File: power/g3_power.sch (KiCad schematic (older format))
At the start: 40 parts, among them J101 533980271_Molex, J102 533980271_Molex, J103 53398-0871, SW1 SW_Push, U101 RT9471GQW, U102 TPS61202DRC, U103 LM358, U104 MCP3422

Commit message: fixes to schematic and layout
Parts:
- added TP101, TP102, TP103, TP104, TP105, TP106, TP107, TP108, TP109, TP110, TP111, TP112, TP113, TP114, TP115: TestPoint, Perch:HARWIN_S2751-46R, symbol Connector:TestPoint
- SW1: symbol Switch:SW_Push -> Switch:SW_DIP_x02
- renumbered R109 to R107, R110 to R108, R111 to R109, R112 to R110
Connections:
- net +5V: now also TP106.1
- net BOOST_PS: now also TP110.1
- net BOOST_VAUX: now also TP101.1
- net CC_PIMD: now also TP104.1
- net CC_PWR_OUT: now also TP102.1
- net CC_SCL: now also TP108.1
- net CC_SDA: now also TP109.1
- net GND: now also SW1.4, TP113.1, TP114.1, TP115.1; no longer H101.1, H102.1, H103.1, H104.1, SW1.2
- net V_BATT: now also TP107.1
- net V_REGN: now also TP105.1
- net V_SOL: now also TP103.1
- net ~CC_CE: now also TP112.1
- net ~CC_INT: now also TP111.1
- no-connect marks 2 -> 8
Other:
- note added: "Test Points"

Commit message: Rerouting power PCB
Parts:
- U102: footprint Package_SON:Texas_S-PVSON-N10_ThermalVias -> digikey-footprints:VSON-10-1EP_3x3mm
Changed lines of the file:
@@
 F 0 "U102" H 9275 3842 50  0000 C CNN
 F 1 "TPS61202DRC" H 9275 3751 50  0000 C CNN
-F 2 "Package_SON:Texas_S-PVSON-N10_ThermalVias" H 9275 2925 50  0001 C CNN
+F 2 "digikey-footprints:VSON-10-1EP_3x3mm" H 9275 2925 50  0001 C CNN
 F 3 "http://www.ti.com/lit/ds/symlink/tps61200.pdf" H 9275 3375 50  0001 C CNN
 	1    9275 3375
@@
 $EndComp
 $Comp
-L custom_power:CC_PWR_OUT #PWR0115
+L g3_power-rescue:CC_PWR_OUT-custom_power #PWR0115
 U 1 1 62098452
 P 1250 6300
@@
 $EndComp
 $Comp
-L custom_power:CC_PWR_OUT #PWR0117
+L g3_power-rescue:CC_PWR_OUT-custom_power #PWR0117
 U 1 1 62098FD7
 P 950 6300
@@
 $EndComp
 $Comp
-L custom_power:CC_PIMD #PWR0121
+L g3_power-rescue:CC_PIMD-custom_power #PWR0121
 U 1 1 620AAC46
 P 2300 6300
@@
 $EndComp
 $Comp
-L custom_power:CC_PWR_OUT #PWR0132
+L g3_power-rescue:CC_PWR_OUT-custom_power #PWR0132
 U 1 1 620C5643
 P 1300 3500
@@
 $EndComp
 $Comp
-L custom_power:CC_PWR_OUT #PWR0133
+L g3_power-rescue:CC_PWR_OUT-custom_power #PWR0133
 U 1 1 620C5BAD
 P 4950 1775
@@
 $EndComp
 $Comp
-L custom_power:BOOST_VAUX #PWR0148
+L g3_power-rescue:BOOST_VAUX-custom_power #PWR0148
 U 1 1 620D33DE
 P 4450 6275
@@
 $EndComp
 $Comp
-L custom_power:BOOST_VAUX #PWR0150
+L g3_power-rescue:BOOST_VAUX-custom_power #PWR0150
 U 1 1 620DC5AE
 P 8000 3425
@@
 $EndComp
 $Comp
-L custom_power:CC_PWR_OUT #PWR0151
+L g3_power-rescue:CC_PWR_OUT-custom_power #PWR0151
 U 1 1 620DD237
 P 8000 3125
@@
 	8000 3475 8875 3475
 $Comp
-L custom_power:BOOST_VAUX #PWR0152
+L g3_power-rescue:BOOST_VAUX-custom_power #PWR0152
 U 1 1 620EE8BF
 P 10100 3225
@@
 	10100 3375 10100 3225
 $Comp
-L custom_power:CC_PWR_OUT #PWR0153
+L g3_power-rescue:CC_PWR_OUT-custom_power #PWR0153
 U 1 1 62018816
 P 1825 3500
@@
 $EndComp
 $Comp
-L custom_power:CC_PIMD #PWR0154
+L g3_power-rescue:CC_PIMD-custom_power #PWR0154
 U 1 1 620415CA
 P 3125 1300
@@
 	5600 6450 5600 6300
 $Comp
-L custom_power:CC_PWR_OUT #PWR0106
+L g3_power-rescue:CC_PWR_OUT-custom_power #PWR0106
 U 1 1 620113D1
 P 5600 6300
@@
 NoConn ~ 5225 5575
 $Comp
-L custom_power:BOOST_VAUX #PWR0155
+L g3_power-rescue:BOOST_VAUX-custom_power #PWR0155
 U 1 1 62184ADE
 P 6200 825
@@
 $EndComp
 $Comp
-L custom_power:CC_PWR_OUT #PWR0156
+L g3_power-rescue:CC_PWR_OUT-custom_power #PWR0156
 U 1 1 621D276E
 P 6200 1100
@@
 $EndComp
 $Comp
-L custom_power:CC_PIMD #PWR0158
+L g3_power-rescue:CC_PIMD-custom_power #PWR0158
 U 1 1 62224531
 P 6200 1700

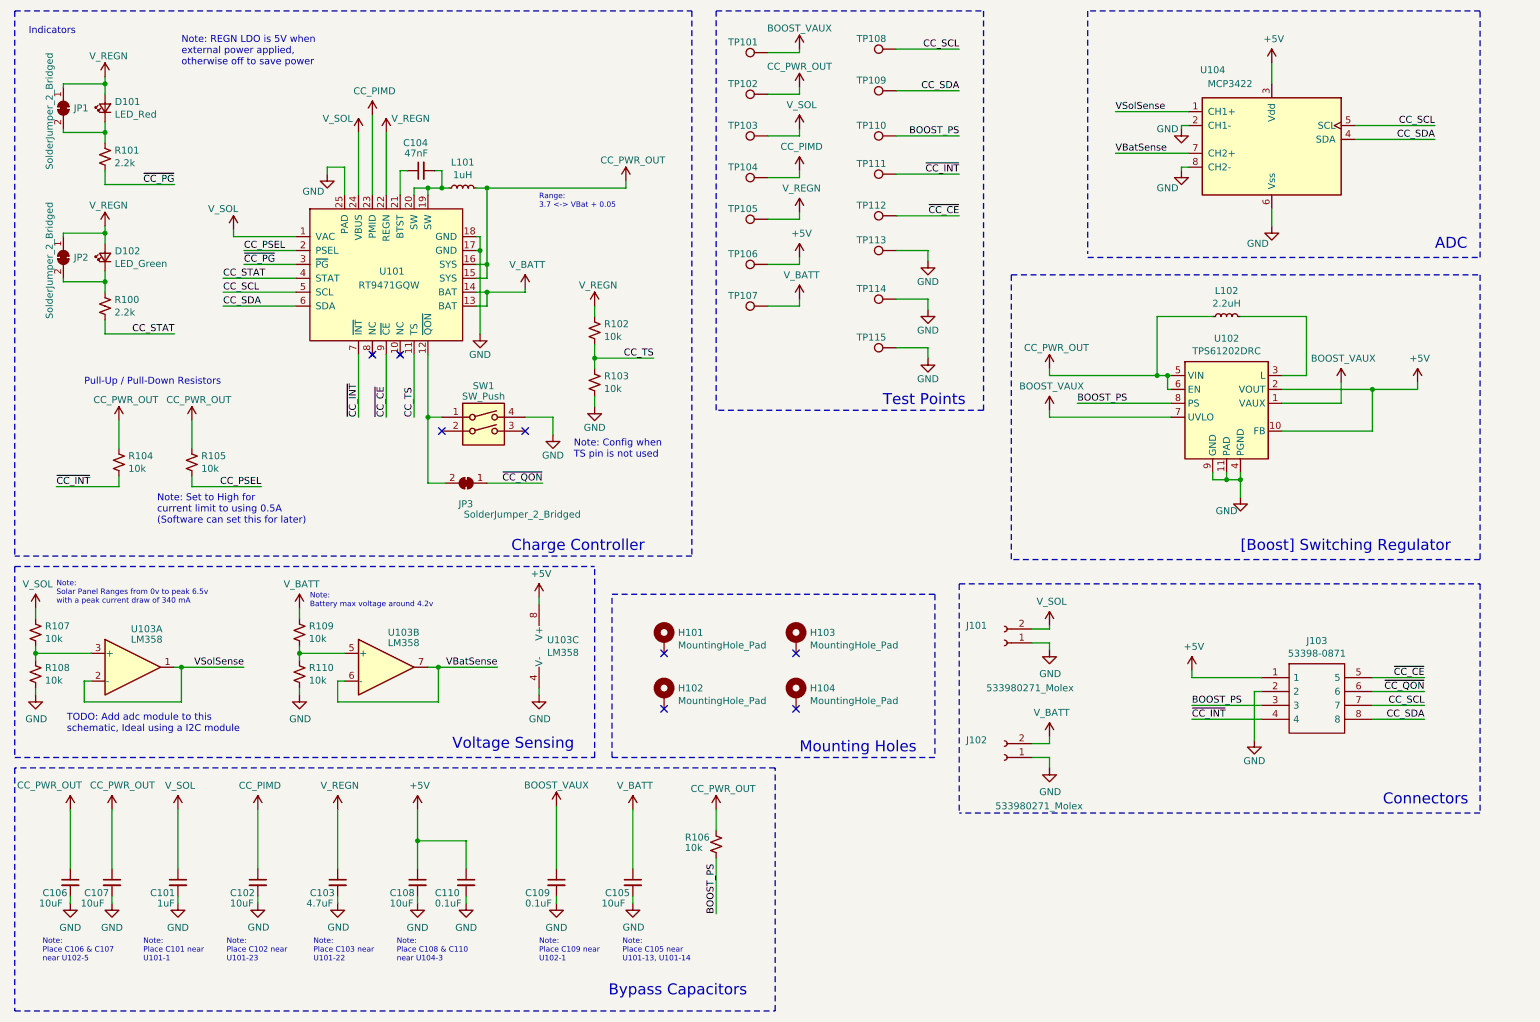
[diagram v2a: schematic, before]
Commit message: Labeling testpoints
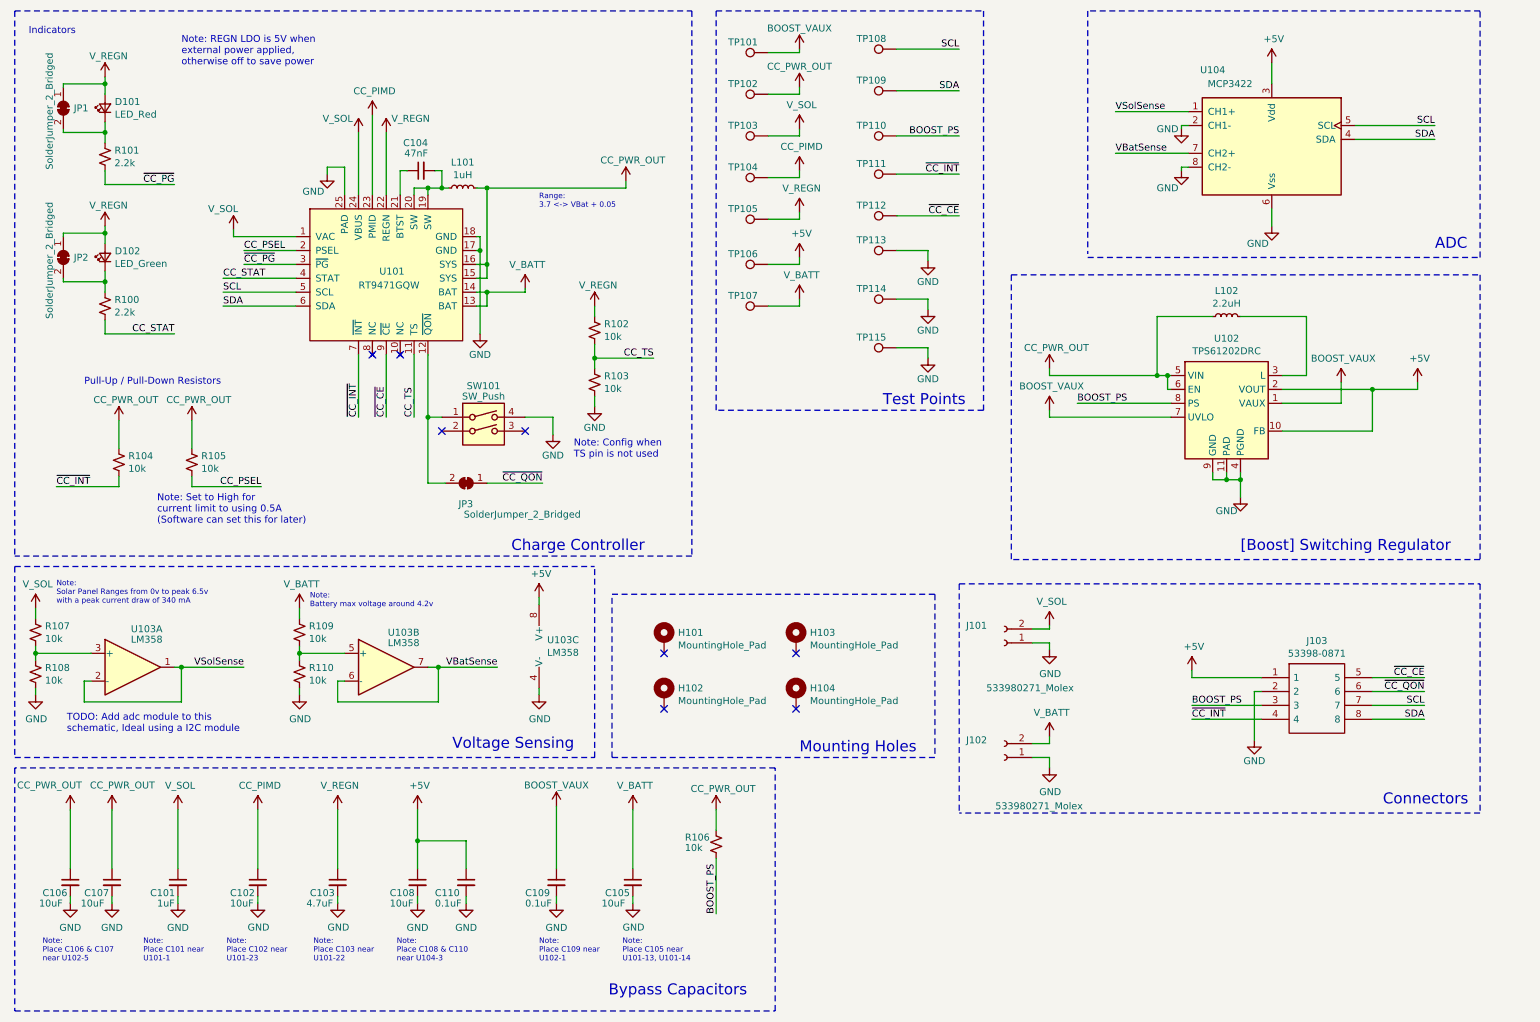
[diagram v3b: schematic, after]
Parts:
- C101, C102, C103, C105, C106, C107, C108, C109, C110: footprint Capacitor_SMD:C_0603_1608Metric_Pad1.08x0.95mm_HandSolder -> Capacitor_SMD:C_0402_1005Metric_Pad0.74x0.62mm_HandSolder
- renumbered SW1 to SW101
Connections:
- net CC_SCL renamed SCL
- net CC_SDA renamed SDA
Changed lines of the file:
@@
 ~CC_QON
 Text Label 10700 5550 2    50   ~ 0
-CC_SCL
+SCL
 Text Label 10700 5650 2    50   ~ 0
-CC_SDA
+SDA
 Wire Notes Line
 	7350 4675 11100 4675
@@
 $EndComp
 $Comp
-L Switch:SW_DIP_x02 SW1
+L Switch:SW_DIP_x02 SW101
 U 1 1 61F2D61E
 P 3925 3575
-F 0 "SW1" H 3925 3900 50  0000 C CNN
+F 0 "SW101" H 3925 3900 50  0000 C CNN
 F 1 "SW_Push" H 3925 3825 50  0000 C CNN
 F 2 "digikey-footprints:Switch_Tactile_SMD_6x6mm_PTS645" H 3925 3775 50  0001 C CNN
@@
 F 0 "C107" H 1050 6750 50  0000 L CNN
 F 1 "10uF" H 1025 6675 50  0000 L CNN
-F 2 "Capacitor_SMD:C_0603_1608Metric_Pad1.08x0.95mm_HandSolder" H 1250 6825 50  0001 C CNN
+F 2 "Capacitor_SMD:C_0402_1005Metric_Pad0.74x0.62mm_HandSolder" H 1250 6825 50  0001 C CNN
 F 3 "~" H 1250 6825 50  0001 C CNN
 	1    1250 6825
@@
 F 0 "C106" H 750 6750 50  0000 L CNN
 F 1 "10uF" H 725 6675 50  0000 L CNN
-F 2 "Capacitor_SMD:C_0603_1608Metric_Pad1.08x0.95mm_HandSolder" H 950 6825 50  0001 C CNN
+F 2 "Capacitor_SMD:C_0402_1005Metric_Pad0.74x0.62mm_HandSolder" H 950 6825 50  0001 C CNN
 F 3 "~" H 950 6825 50  0001 C CNN
 	1    950  6825
@@
 F 0 "C101" H 1525 6750 50  0000 L CNN
 F 1 "1uF" H 1575 6675 50  0000 L CNN
-F 2 "Capacitor_SMD:C_0603_1608Metric_Pad1.08x0.95mm_HandSolder" H 1725 6825 50  0001 C CNN
+F 2 "Capacitor_SMD:C_0402_1005Metric_Pad0.74x0.62mm_HandSolder" H 1725 6825 50  0001 C CNN
 F 3 "~" H 1725 6825 50  0001 C CNN
 F 4 "" H 1725 6825 50  0001 C CNN "MFN"
@@
 F 0 "C102" H 2100 6750 50  0000 L CNN
 F 1 "10uF" H 2100 6675 50  0000 L CNN
-F 2 "Capacitor_SMD:C_0603_1608Metric_Pad1.08x0.95mm_HandSolder" H 2300 6825 50  0001 C CNN
+F 2 "Capacitor_SMD:C_0402_1005Metric_Pad0.74x0.62mm_HandSolder" H 2300 6825 50  0001 C CNN
 F 3 "~" H 2300 6825 50  0001 C CNN
 F 4 "" H 2300 6825 50  0001 C CNN "MFN"
@@
 F 0 "C103" H 2675 6750 50  0000 L CNN
 F 1 "4.7uF" H 2650 6675 50  0000 L CNN
-F 2 "Capacitor_SMD:C_0603_1608Metric_Pad1.08x0.95mm_HandSolder" H 2875 6825 50  0001 C CNN
+F 2 "Capacitor_SMD:C_0402_1005Metric_Pad0.74x0.62mm_HandSolder" H 2875 6825 50  0001 C CNN
 F 3 "~" H 2875 6825 50  0001 C CNN
 F 4 "" H 2875 6825 50  0001 C CNN "MFN"
@@
 CC_PSEL
 Text Label 2050 2575 0    50   ~ 0
-CC_SCL
+SCL
 Text Label 2050 2675 0    50   ~ 0
-CC_SDA
+SDA
 Text Label 3025 3475 1    50   ~ 0
 ~CC_INT
@@
 $EndComp
 Text Label 10775 1475 2    50   ~ 0
-CC_SDA
+SDA
 Wire Wire Line
 	10200 1375 10775 1375
@@
 	10200 1475 10775 1475
 Text Label 10775 1375 2    50   ~ 0
-CC_SCL
+SCL
 $Comp
 L power:GND #PWR0140
@@
 F 0 "C108" H 3250 6750 50  0000 L CNN
 F 1 "10uF" H 3250 6675 50  0000 L CNN
-F 2 "Capacitor_SMD:C_0603_1608Metric_Pad1.08x0.95mm_HandSolder" H 3450 6825 50  0001 C CNN
+F 2 "Capacitor_SMD:C_0402_1005Metric_Pad0.74x0.62mm_HandSolder" H 3450 6825 50  0001 C CNN
 F 3 "~" H 3450 6825 50  0001 C CNN
 F 4 "" H 3450 6825 50  0001 C CNN "MFN"
@@
 F 0 "C110" H 3575 6750 50  0000 L CNN
 F 1 "0.1uF" H 3575 6675 50  0000 L CNN
-F 2 "Capacitor_SMD:C_0603_1608Metric_Pad1.08x0.95mm_HandSolder" H 3800 6825 50  0001 C CNN
+F 2 "Capacitor_SMD:C_0402_1005Metric_Pad0.74x0.62mm_HandSolder" H 3800 6825 50  0001 C CNN
 F 3 "~" H 3800 6825 50  0001 C CNN
 F 4 "" H 3800 6825 50  0001 C CNN "MFN"
@@
 F 0 "C109" H 4225 6750 50  0000 L CNN
 F 1 "0.1uF" H 4225 6675 50  0000 L CNN
-F 2 "Capacitor_SMD:C_0603_1608Metric_Pad1.08x0.95mm_HandSolder" H 4450 6825 50  0001 C CNN
+F 2 "Capacitor_SMD:C_0402_1005Metric_Pad0.74x0.62mm_HandSolder" H 4450 6825 50  0001 C CNN
 F 3 "~" H 4450 6825 50  0001 C CNN
 F 4 "" H 4450 6825 50  0001 C CNN "MFN"
@@
 F 0 "C105" H 4800 6750 50  0000 L CNN
 F 1 "10uF" H 4775 6675 50  0000 L CNN
-F 2 "Capacitor_SMD:C_0603_1608Metric_Pad1.08x0.95mm_HandSolder" H 5000 6825 50  0001 C CNN
+F 2 "Capacitor_SMD:C_0402_1005Metric_Pad0.74x0.62mm_HandSolder" H 5000 6825 50  0001 C CNN
 F 3 "~" H 5000 6825 50  0001 C CNN
 	1    5000 6825
@@
 	6900 825  7350 825
 Text Label 7350 825  2    50   ~ 0
-CC_SCL
+SCL
 Wire Wire Line
 	6900 1125 7350 1125
@@
 	6900 1450 7350 1450
 Text Label 7350 1125 2    50   ~ 0
-CC_SDA
+SDA
 Wire Wire Line
 	6900 2275 7125 2275

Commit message: added part numbers
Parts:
- C101: Description (none) -> 1uF Capacitor; MFN (none) -> Yageo; MFP (none) -> CC0402MRX5R6BB105; Manufacturer_Name (none) -> Yageo; Manufacturer_Part_Number (none) -> CC0402MRX5R6BB105; S1PL (none) -> https://www.digikey.com/en/products/detail/yageo/CC0402MRX5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; S1PN (none) -> 311-1732
- C102, C105, C106, C107, C108: Description (none) -> 10uF Capacitor; MFN (none) -> Yageo; MFP (none) -> CAP CER 10000PF 16V X7R 0402; Manufacturer_Name (none) -> Yageo; Manufacturer_Part_Number (none) -> CAP CER 10000PF 16V X7R 0402; S1PL (none) -> https://www.digikey.com/en/products/detail/yageo/CC0402KPX7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; S1PN (none) -> 13-CC0402KPX7R7BB103
- C103: Description (none) -> 4.7uF Capacitor; MFN (none) -> Yageo; MFP (none) -> CC0402MRX5R6BB475; Manufacturer_Name (none) -> Yageo; Manufacturer_Part_Number (none) -> CC0402MRX5R6BB475; S1PL (none) -> https://www.digikey.com/en/products/detail/yageo/CC0402MRX5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; S1PN (none) -> 311-1734
- C104: Description (none) -> 47nF Capacitor; MFN (none) -> Samsung; MFP (none) -> CL21B473KCCWPNC; Manufacturer_Name (none) -> Samsung; Manufacturer_Part_Number (none) -> CL21B473KCCWPNC; S1PL (none) -> https://www.digikey.com/en/products/detail/samsung-electro-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; S1PN (none) -> 1276-6815
- C109, C110: Description (none) -> 0.1uF Capacitor; MFN (none) -> Yageo; MFP (none) -> CC0402JRX7R7BB104; Manufacturer_Name (none) -> Yageo; Manufacturer_Part_Number (none) -> CC0402JRX7R7BB104; S1PL (none) -> https://www.digikey.com/en/products/detail/yageo/CC0402JRX7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; S1PN (none) -> 311-1676
- D101: Description (none) -> LED Red; MFN (none) -> Lumex Opto/Components Inc.; MFP (none) -> SML-LX0402SIC-TR; Manufacturer_Name (none) -> Lumex Opto/Components Inc.; Manufacturer_Part_Number (none) -> SML-LX0402SIC-TR; S1PL (none) -> https://www.digikey.com/en/products/detail/lumex-opto-compo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; S1PN (none) -> 67-1878
- D102: Description (none) -> LED Green; MFN (none) -> Lumex Opto/Components Inc.; MFP (none) -> SML-LX0402SUGC-TR; Manufacturer_Name (none) -> Lumex Opto/Components Inc.; Manufacturer_Part_Number (none) -> SML-LX0402SUGC-TR; S1PL (none) -> https://www.digikey.com/en/products/detail/lumex-opto-compo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; S1PN (none) -> 67-1881
- J101, J102: Description (none) -> 2 Pin Molex Header; MFN (none) -> Molex; MFP (none) -> 532610271; Manufacturer_Name (none) -> Molex; Manufacturer_Part_Number (none) -> 532610271; S1PL (none) -> https://www.heilind.com/mol53261-0271-p.html; S1PN (none) -> MOL53261-0271
- J103: Description 8 way straight SMT header,1.25mm pitch Molex PICOBLADE Seri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 -> 8 Pin Molex Header; MFN (none) -> Molex; MFP (none) -> 533980871; Manufacturer_Part_Number 53398-0871 -> 533980871; S1PL (none) -> https://www.heilind.com/search/result?q=53398-0871&manufact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; S1PN (none) -> MOL53398-0871
- L101: Description (none) -> 1uH Inductor; MFN (none) -> Samsung; MFP (none) -> CIGT252010LM1R0MNE; Manufacturer_Name (none) -> Samsung; Manufacturer_Part_Number (none) -> CIGT252010LM1R0MNE; S1PL (none) -> https://www.digikey.com/en/products/detail/samsung-electro-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; S1PN (none) -> 1276-6939
- L102: Description (none) -> 2.2uH Inductor; MFN (none) -> Samsung; MFP (none) -> CIGT201610LH2R2MNE; Manufacturer_Name (none) -> Samsung; Manufacturer_Part_Number (none) -> CIGT201610LH2R2MNE; S1PL (none) -> https://www.digikey.com/en/products/detail/samsung-electro-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; S1PN (none) -> 1276-6911
- R100, R101: Description (none) -> 2.2k Resistor; MFN (none) -> Yageo; MFP (none) -> RC0402JR-072K2L; Manufacturer_Name (none) -> Yageo; Manufacturer_Part_Number (none) -> RC0402JR-072K2L; S1PL (none) -> https://www.digikey.com/en/products/detail/yageo/RC0402JR-0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; S1PN (none) -> 311-2.2KJRTR
- R102, R103, R104, R105, R106, R107, R108, R109, R110: Description (none) -> 10k Resistor; MFN (none) -> Yageo; MFP (none) -> RC0402JR-0710KL; Manufacturer_Name (none) -> Yageo; Manufacturer_Part_Number (none) -> RC0402JR-0710KL; S1PL (none) -> digikey.com/en/products/detail/yageo/RC0402JR-0710KL/726418; S1PN (none) -> 311-10KJRTR
- SW101: Description (none) -> Tactile switch; MFN (none) -> C&K; MFP (none) -> PTS645SH43SMTR92 LFS; Manufacturer_Name (none) -> C&K; Manufacturer_Part_Number (none) -> PTS645SH43SMTR92 LFS; S1PL (none) -> https://www.digikey.com/en/products/detail/c-k/PTS645SH43SM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; S1PN (none) -> CKN11907TR
- U101: Manufacturer_Name (none) -> Richtek USA Inc.; Manufacturer_Part_Number (none) -> RT9471GQW(2)
- U102: Description (none) -> Switching Regulator; MFN (none) -> Texas Instruments; MFP (none) -> TPS61202DRCT; Manufacturer_Name (none) -> Texas Instruments; Manufacturer_Part_Number (none) -> TPS61202DRCT; S1PL (none) -> https://www.digikey.com/en/products/detail/texas-instrument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; S1PN (none) -> 296-21685
- U103: Description (none) -> Dual operational amplifiers; MFN (none) -> STMicroelectronics; MFP (none) -> LM358D; Manufacturer_Name (none) -> STMicroelectronics; Manufacturer_Part_Number (none) -> LM358D; S1PL (none) -> https://www.digikey.com/en/products/detail/stmicroelectroni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; S1PN (none) -> 497-18378
- U104: Description (none) -> 18 Bit Dual ADC; MFN (none) -> Microchip Technology; MFP (none) -> MCP3422A1T-E/SN; Manufacturer_Name (none) -> Microchip Technology; Manufacturer_Part_Number (none) -> MCP3422A1T-E/SN; S1PL (none) -> https://www.digikey.com/en/products/detail/microchip-techno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; S1PN (none) -> MCP3422A1T-E
